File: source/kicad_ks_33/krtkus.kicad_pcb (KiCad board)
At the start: 2 copper layers, 232.6 x 118.3 mm, 123 parts, among them SW1 Push, SW10 Push, SW11 Push, SW12 Push, SW14 Push, SW15 Push, SW16 Push, SW17 Push, SW18 Push, SW2 Push, SW20 Push, SW21 Push, SW22 Push, SW23 Push, SW24 Push, SW26 Push, SW27 Push, SW28 Push, SW29 Push, SW3 Push, SW30 Push, SW32 Push, SW33 Push, SW34 Push, SW35 Push, SW38 Push, SW39 Push, SW4 Push, SW40 Push, SW41 Push, SW42 Push, SW44 Push, SW45 Push, SW46 Push, SW47 Push, SW48 Push, SW5 Push, SW50 Push, SW51 Push, SW52 Push, SW53 Push, SW54 Push, SW56 Push, SW57 Push, SW58 Push, SW59 Push, SW6 Push, SW60 Push, SW62 Push, SW63 Push, SW64 Push, SW65 Push, SW66 Push, SW67 Push, SW68 Push, SW69 Push, SW70 Push, SW71 Push, SW72 Push, SW8 Push, SW9 Push, U1 Arduino_Pro_Micro

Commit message: unification
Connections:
- U1 pad 1: COL1 -> COL5
- U1 pad 10: ROW2 -> COL7
- U1 pad 11: COL7 -> COL9
- U1 pad 15: COL9 -> ROW2
- U1 pad 16: COL6 -> ROW1
- U1 pad 17: COL5 -> ROW0
- U1 pad 18: COL4 -> ROW3
- U1 pad 19: COL3 -> ROW4
- U1 pad 2: COL0 -> COL4
- U1 pad 20: COL2 -> ROW5
- U1 pad 5: ROW5 -> COL3
- U1 pad 6: ROW4 -> COL2
- U1 pad 7: ROW3 -> COL1
- U1 pad 8: ROW0 -> COL0
- U1 pad 9: ROW1 -> COL6
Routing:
- net ROW2: track 271.9 -> 317.9 mm, vias 14 -> 13
- net ROW3: track 292.7 -> 322.4 mm, vias 14 -> 15
- net ROW1: track 252.9 -> 281.4 mm, vias 12 -> 13
- net COL5: track 132.3 -> 103.9 mm
- net ROW4: track 322.1 -> 342.8 mm, vias 14 -> 15
- net COL4: track 170.3 -> 151.4 mm
- net COL0: track 249.9 -> 267.3 mm, vias 1 -> 0
- net COL1: track 211.8 -> 228.0 mm, vias 1 -> 0
- net COL6: track 145.2 -> 132.8 mm
- net ROW0: track 228.9 -> 219.0 mm
- net ROW5: track 353.0 -> 362.0 mm, vias 13 -> 14
- net COL7: track 120.4 -> 112.0 mm
- net COL3: track 187.4 -> 181.3 mm
- net COL9: track 146.7 -> 140.9 mm
- net COL2: track 202.8 -> 204.4 mm

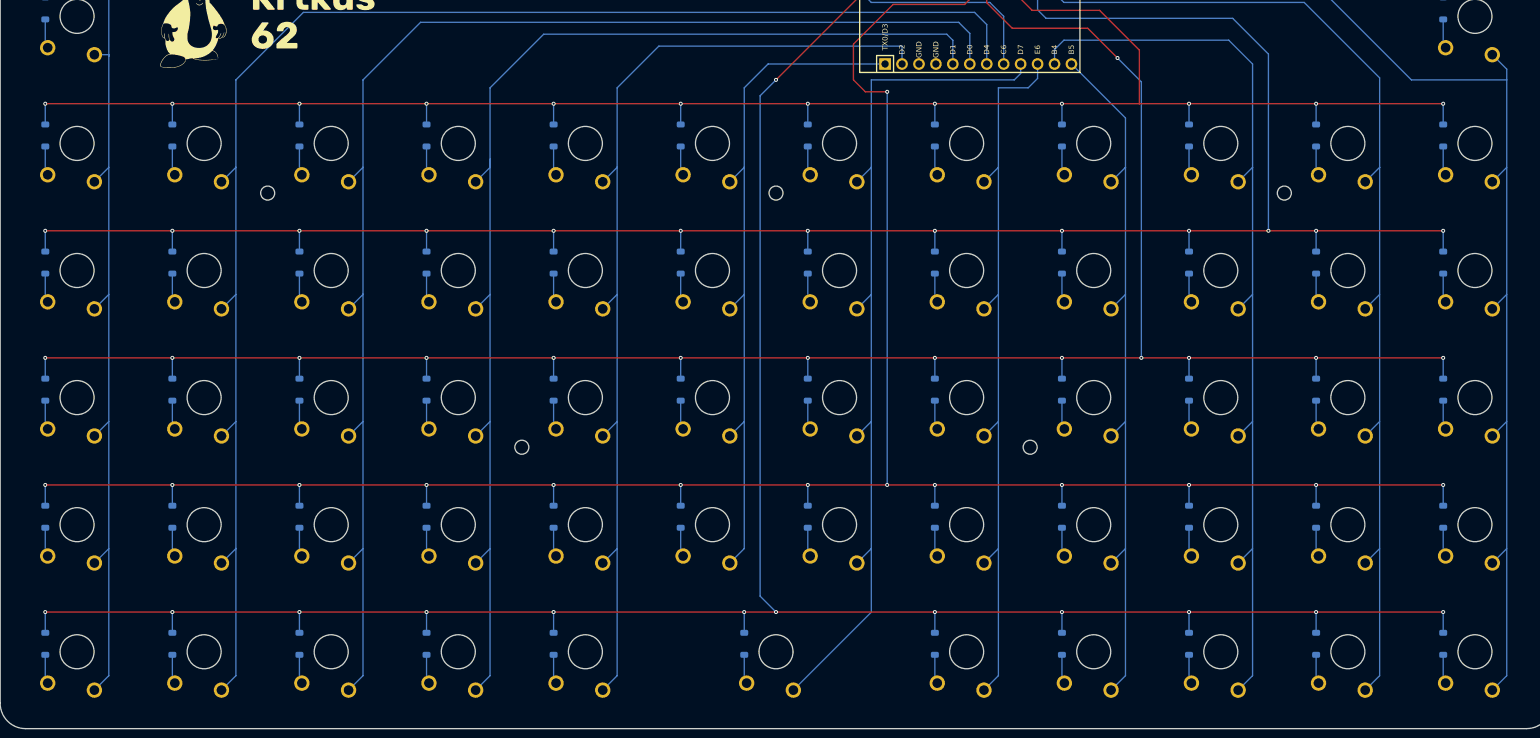
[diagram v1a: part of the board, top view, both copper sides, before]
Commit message: ks-33 footprint tweaks
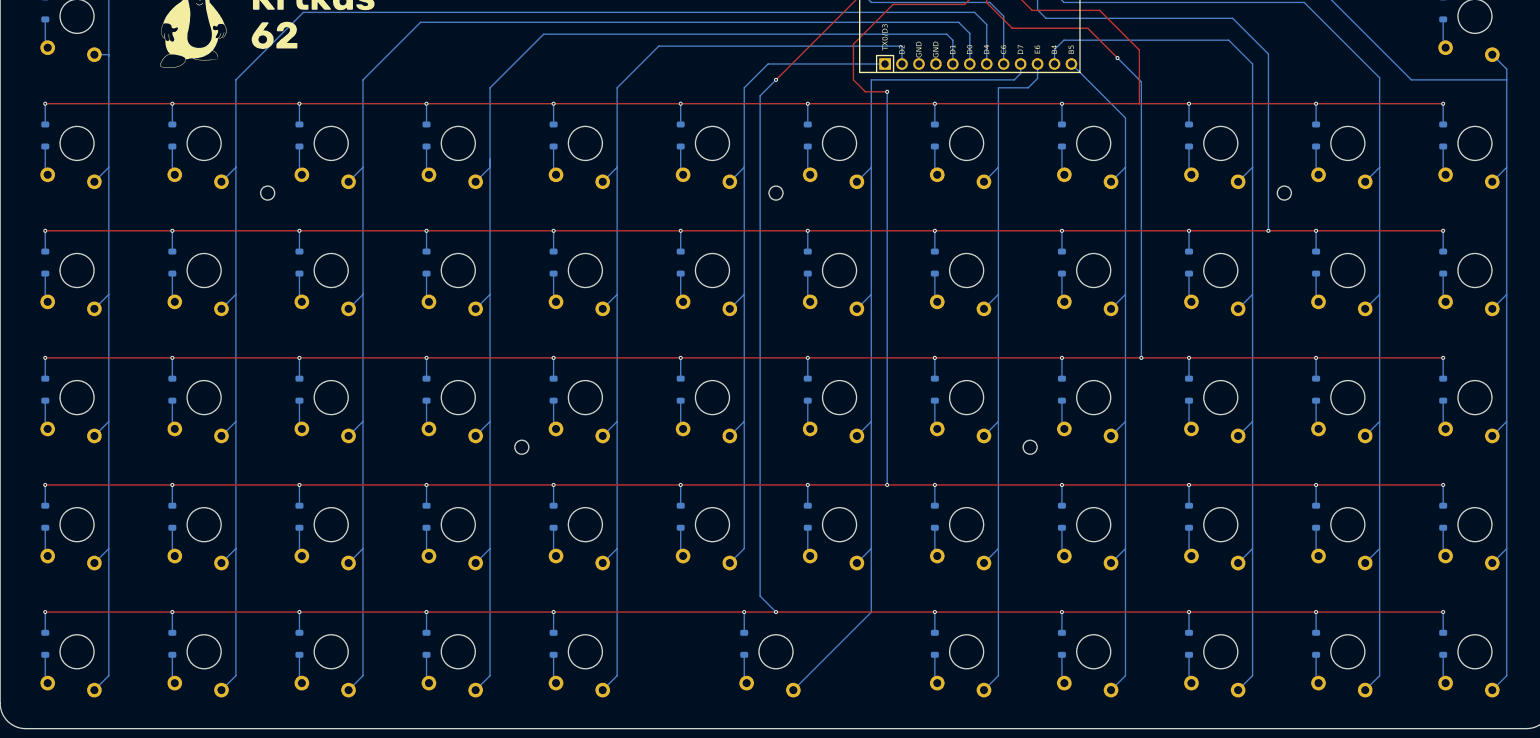
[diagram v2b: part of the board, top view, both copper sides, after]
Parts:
- SW1, SW10, SW11, SW12, SW14, SW15, SW16, SW17, SW18, SW2, SW20, SW21, SW22, SW23, SW24, SW26, SW27, SW28, SW29, SW3, SW30, SW32, SW33, SW34, SW35, SW38, SW39, SW4, SW40, SW41, SW42, SW44, SW45, SW46, SW47, SW48, SW5, SW50, SW51, SW52, SW53, SW54, SW56, SW57, SW58, SW59, SW6, SW60, SW62, SW63, SW64, SW65, SW66, SW67, SW68, SW69, SW70, SW71, SW72, SW8, SW9: footprint Gateron_KS33_Solderable:Gateron-KS33-Solderable-1U -> Gateron_KS33_Solderable:Gateron-KS33-Solderable-1U-Tight
